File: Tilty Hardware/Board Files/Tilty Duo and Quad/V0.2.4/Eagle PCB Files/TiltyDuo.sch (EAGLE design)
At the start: 45 parts, among them U1 TEENSY_3.0_OUTER-PINS28-DIP_S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, U2 HC-09_BREAKOUT, U3 MPL3115A2LGA8, U4 LM2931, U5 MPU-6050, U6 HMC5883LSMD, U7 SPI_FLASH-X25XXSMD

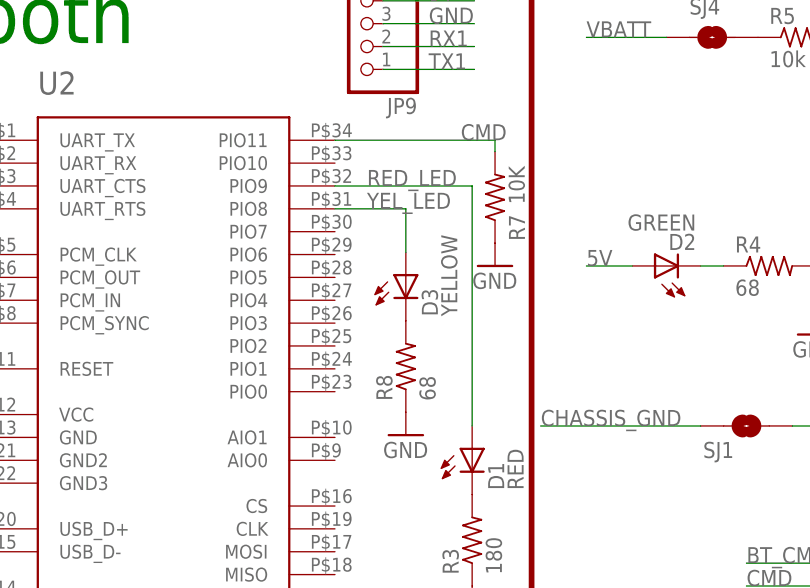
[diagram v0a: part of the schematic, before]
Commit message: Tweaked LED order on Duo/Quad, added lots of memory testing (libraries to come soon)
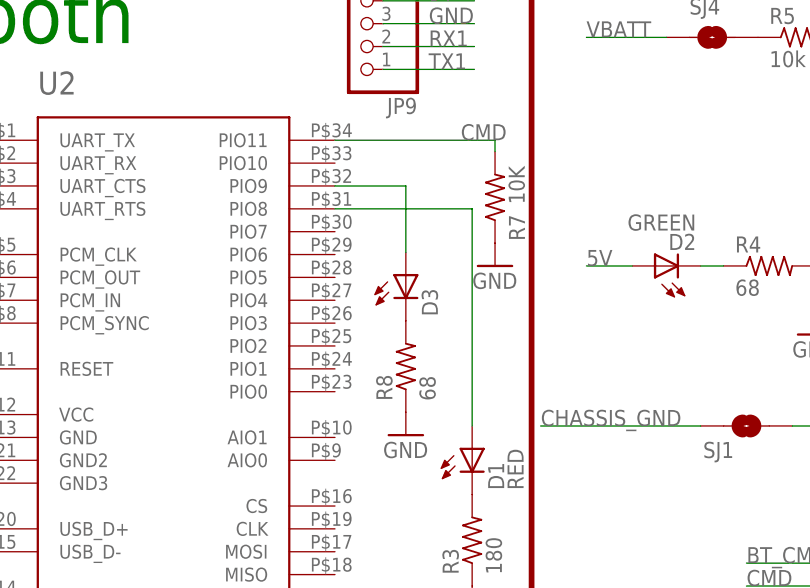
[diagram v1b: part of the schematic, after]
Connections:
- removed net RED_LED: D1.A, U2.PIO9
- new net N$14: D1.A, U2.PIO8
- net YEL_LED: now also U2.PIO9; no longer U2.PIO8
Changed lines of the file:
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@@
 <?xml version="1.0" encoding="utf-8"?>
 <!DOCTYPE eagle SYSTEM "eagle.dtd">
-<eagle version="6.4">
+<eagle version="6.5.0">
 <drawing>
 <settings>
@@
 <instance part="D3" gate="G$1" x="73.914" y="42.164" smashed="yes">
 <attribute name="NAME" x="77.47" y="37.592" size="1.778" layer="95" rot="R90"/>
-<attribute name="VALUE" x="79.629" y="37.592" size="1.778" layer="96" rot="R90"/>
 </instance>
 <instance part="GND7" gate="1" x="73.914" y="24.384"/>
@@
 </segment>
 </net>
-<net name="RED_LED" class="0">
-<segment>
+<net name="YEL_LED" class="0">
+<segment>
+<pinref part="D3" gate="G$1" pin="A"/>
+<wire x1="73.914" y1="52.07" x2="73.914" y2="44.704" width="0.1524" layer="91"/>
 <pinref part="U2" gate="G$1" pin="PIO9"/>
-<wire x1="66.04" y1="52.07" x2="81.28" y2="52.07" width="0.1524" layer="91"/>
-<label x="69.596" y="52.07" size="1.778" layer="95"/>
-<pinref part="D1" gate="G$1" pin="A"/>
-<wire x1="81.28" y1="25.4" x2="81.28" y2="52.07" width="0.1524" layer="91"/>
-</segment>
-</net>
-<net name="YEL_LED" class="0">
-<segment>
-<pinref part="U2" gate="G$1" pin="PIO8"/>
-<wire x1="66.04" y1="49.53" x2="73.914" y2="49.53" width="0.1524" layer="91"/>
-<label x="69.596" y="49.53" size="1.778" layer="95"/>
-<pinref part="D3" gate="G$1" pin="A"/>
-<wire x1="73.914" y1="49.53" x2="73.914" y2="44.704" width="0.1524" layer="91"/>
+<wire x1="73.914" y1="52.07" x2="66.04" y2="52.07" width="0.1524" layer="91"/>
 </segment>
 </net>
@@
 </segment>
 </net>
+<net name="N$14" class="0">
+<segment>
+<pinref part="D1" gate="G$1" pin="A"/>
+<wire x1="81.28" y1="25.4" x2="81.28" y2="49.53" width="0.1524" layer="91"/>
+<pinref part="U2" gate="G$1" pin="PIO8"/>
+<wire x1="81.28" y1="49.53" x2="66.04" y2="49.53" width="0.1524" layer="91"/>
+</segment>
+</net>

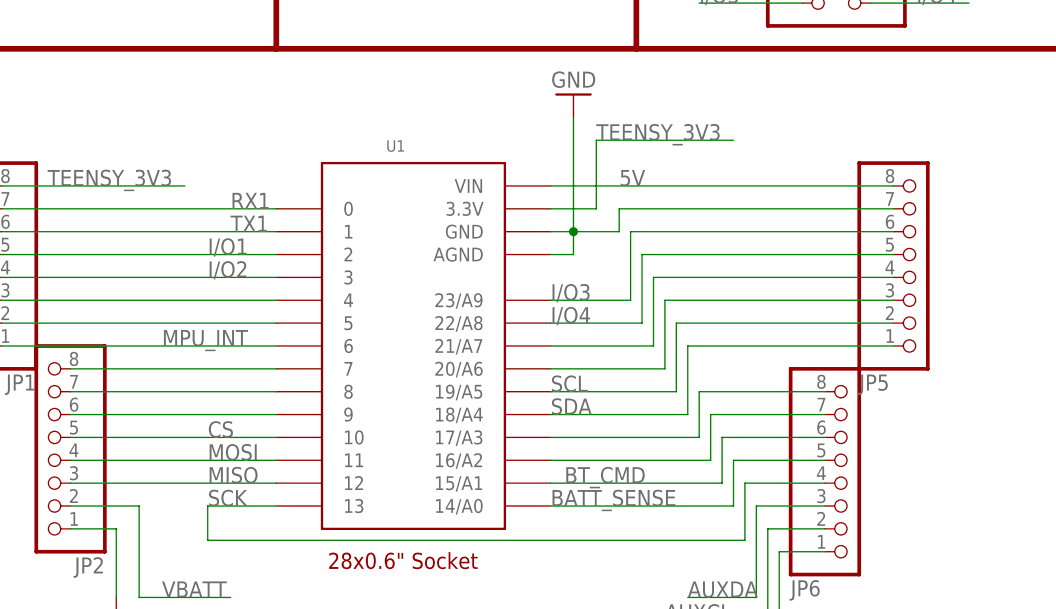
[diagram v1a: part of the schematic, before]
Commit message: Updated Altimeter library to take data pointers as well as return data
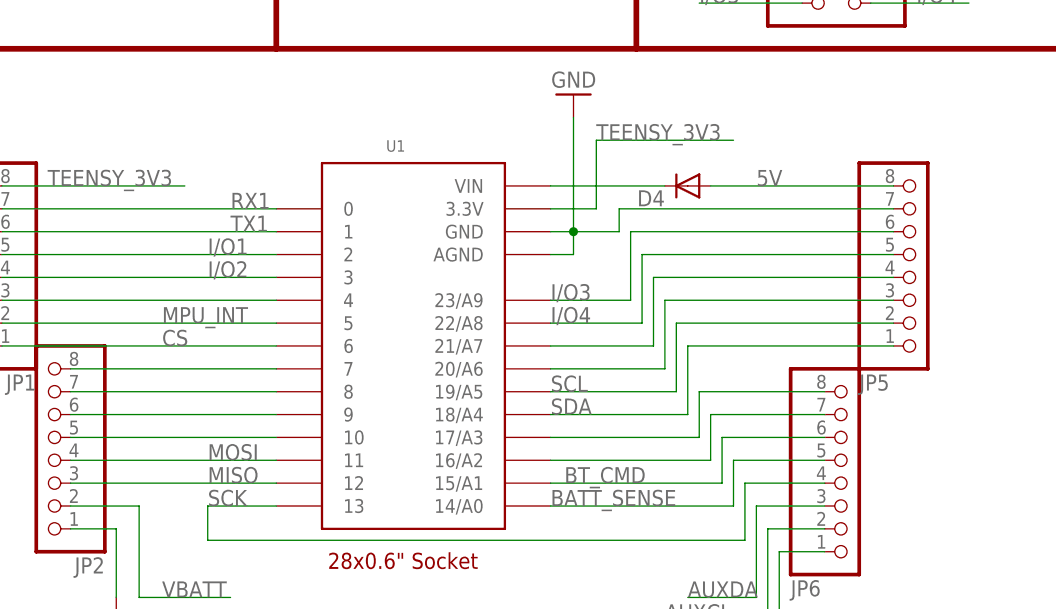
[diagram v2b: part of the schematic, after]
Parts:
- added D4: (no value), SparkFun-DiscreteSemi:DIODESOT23
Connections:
- new net N$15: D4.C, U1.VIN
- net 5V: now also D4.A; no longer U1.VIN
- net CS: now also JP1.1, U1.6; no longer JP2.5, U1.10
- net MPU_INT: now also JP1.2, U1.5; no longer JP1.1, U1.6
- net N$8: now also JP2.5, U1.10; no longer JP1.2, U1.5
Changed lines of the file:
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@@
 <part name="SJ4" library="SparkFun-Passives" deviceset="SOLDERJUMPER" device="TRACE"/>
 <part name="SJ5" library="SparkFun-Passives" deviceset="JUMPER-2" device="SMD-NC"/>
+<part name="D4" library="SparkFun-DiscreteSemi" deviceset="DIODE" device="SOT23"/>
 </parts>
 <sheets>
@@
 </instance>
 <instance part="SJ5" gate="A" x="129.54" y="10.16" rot="R270"/>
+<instance part="D4" gate="G$1" x="218.44" y="60.96" rot="R180"/>
 </instances>
 <busses>
@@
 </segment>
 <segment>
-<pinref part="U1" gate="G$1" pin="6"/>
-<wire x1="172.72" y1="43.18" x2="142.24" y2="43.18" width="0.1524" layer="91"/>
-<pinref part="JP1" gate="A" pin="1"/>
-<label x="160.02" y="43.18" size="1.778" layer="95"/>
+<pinref part="U1" gate="G$1" pin="5"/>
+<wire x1="172.72" y1="45.72" x2="142.24" y2="45.72" width="0.1524" layer="91"/>
+<pinref part="JP1" gate="A" pin="2"/>
+<label x="160.02" y="45.72" size="1.778" layer="95"/>
 </segment>
 </net>
@@
 </segment>
 <segment>
-<pinref part="U1" gate="G$1" pin="VIN"/>
-<pinref part="JP5" gate="A" pin="8"/>
-<wire x1="203.2" y1="60.96" x2="241.3" y2="60.96" width="0.1524" layer="91"/>
-<label x="210.82" y="60.96" size="1.778" layer="95"/>
-</segment>
-<segment>
 <wire x1="99.06" y1="43.18" x2="93.98" y2="43.18" width="0.1524" layer="91"/>
 <label x="93.98" y="43.18" size="1.778" layer="95"/>
@@
 <label x="246.38" y="121.92" size="1.778" layer="95"/>
 </segment>
+<segment>
+<pinref part="D4" gate="G$1" pin="A"/>
+<pinref part="JP5" gate="A" pin="8"/>
+<wire x1="220.98" y1="60.96" x2="241.3" y2="60.96" width="0.1524" layer="91"/>
+<label x="226.06" y="60.96" size="1.778" layer="95"/>
+</segment>
 </net>
 <net name="N$7" class="0">
@@
 <wire x1="172.72" y1="48.26" x2="142.24" y2="48.26" width="0.1524" layer="91"/>
 <pinref part="JP1" gate="A" pin="3"/>
-</segment>
-</net>
-<net name="N$8" class="0">
-<segment>
-<pinref part="U1" gate="G$1" pin="5"/>
-<wire x1="172.72" y1="45.72" x2="142.24" y2="45.72" width="0.1524" layer="91"/>
-<pinref part="JP1" gate="A" pin="2"/>
 </segment>
 </net>
@@
 </segment>
 <segment>
-<pinref part="U1" gate="G$1" pin="10"/>
-<wire x1="149.86" y1="33.02" x2="172.72" y2="33.02" width="0.1524" layer="91"/>
-<pinref part="JP2" gate="A" pin="5"/>
-<label x="165.1" y="33.02" size="1.778" layer="95"/>
+<pinref part="U1" gate="G$1" pin="6"/>
+<wire x1="172.72" y1="43.18" x2="142.24" y2="43.18" width="0.1524" layer="91"/>
+<pinref part="JP1" gate="A" pin="1"/>
+<label x="160.02" y="43.18" size="1.778" layer="95"/>
 </segment>
 </net>
@@
 </segment>
 </net>
+<net name="N$8" class="0">
+<segment>
+<pinref part="JP2" gate="A" pin="5"/>
+<pinref part="U1" gate="G$1" pin="10"/>
+<wire x1="149.86" y1="33.02" x2="172.72" y2="33.02" width="0.1524" layer="91"/>
+</segment>
+</net>
+<net name="N$15" class="0">
+<segment>
+<pinref part="D4" gate="G$1" pin="C"/>
+<pinref part="U1" gate="G$1" pin="VIN"/>
+<wire x1="215.9" y1="60.96" x2="203.2" y2="60.96" width="0.1524" layer="91"/>
+</segment>
+</net>

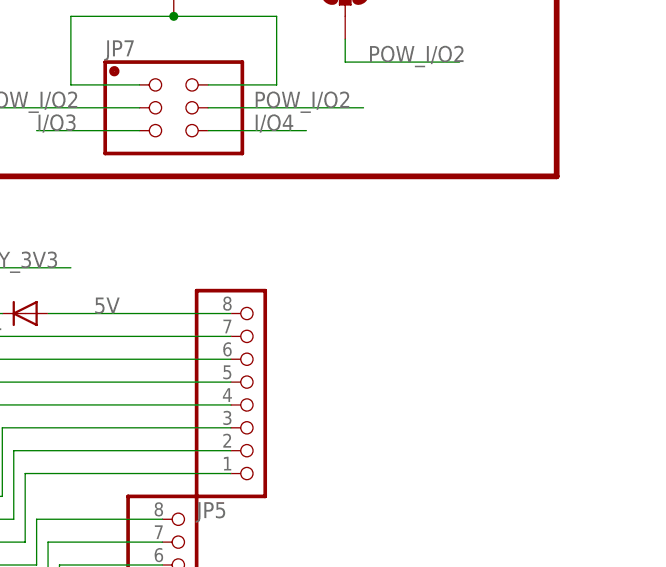
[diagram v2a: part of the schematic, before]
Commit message: Updated Tilty Duo/Quad PCB and TiltyIMU software library
PCB: Added circuit protection
Software: Fixed conflicts with duplicate file names
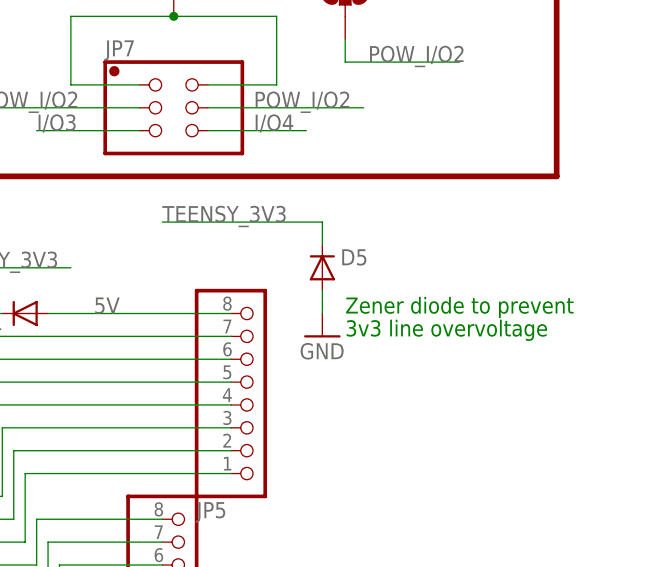
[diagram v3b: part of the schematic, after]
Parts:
- added D5: (no value), SparkFun-DiscreteSemi:DIODESOT23
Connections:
- net GND: now also D5.A
- net TEENSY_3V3: now also D5.C
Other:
- note added: "3v3 line overvoltage"
- note added: "Zener diode to prevent"
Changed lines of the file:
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@@
 <part name="SJ5" library="SparkFun-Passives" deviceset="JUMPER-2" device="SMD-NC"/>
 <part name="D4" library="SparkFun-DiscreteSemi" deviceset="DIODE" device="SOT23"/>
+<part name="D5" library="SparkFun-DiscreteSemi" deviceset="DIODE" device="SOT23">
+<attribute name="PART#" value="BZX84C3V3LT1GOSCT-ND"/>
+</part>
+<part name="GND23" library="supply1" deviceset="GND" device=""/>
 </parts>
 <sheets>
@@
 <wire x1="182.88" y1="193.04" x2="252.222" y2="193.04" width="0.635" layer="94"/>
 <text x="190.5" y="185.42" size="5.08" layer="91" ratio="14">Flash Memory</text>
+<text x="254" y="60.96" size="1.778" layer="91">Zener diode to prevent</text>
+<text x="254" y="58.42" size="1.778" layer="91">3v3 line overvoltage</text>
 </plain>
 <instances>
@@
 <instance part="SJ5" gate="A" x="129.54" y="10.16" rot="R270"/>
 <instance part="D4" gate="G$1" x="218.44" y="60.96" rot="R180"/>
+<instance part="D5" gate="G$1" x="251.46" y="66.04" smashed="yes" rot="R90">
+<attribute name="NAME" x="256.54" y="68.0974" size="1.778" layer="95" rot="R180"/>
+<attribute name="VALUE" x="253.7714" y="68.58" size="1.778" layer="96" rot="R90"/>
+<attribute name="PART#" x="251.46" y="66.04" size="1.778" layer="96" rot="R90" display="off"/>
+</instance>
+<instance part="GND23" gate="1" x="251.46" y="58.42"/>
 </instances>
 <busses>
@@
 <wire x1="190.5" y1="160.02" x2="200.66" y2="160.02" width="0.1524" layer="91"/>
 <junction x="200.66" y="160.02"/>
+</segment>
+<segment>
+<pinref part="D5" gate="G$1" pin="A"/>
+<pinref part="GND23" gate="1" pin="GND"/>
+<wire x1="251.46" y1="60.96" x2="251.46" y2="63.5" width="0.1524" layer="91"/>
 </segment>
 </net>
@@
 <junction x="200.66" y="175.26"/>
 </segment>
-</net>
+<segment>
+<pinref part="D5" gate="G$1" pin="C"/>
+<wire x1="251.46" y1="68.58" x2="251.46" y2="71.12" width="0.1524" layer="91"/>
+<wire x1="251.46" y1="71.12" x2="233.68" y2="71.12" width="0.1524" layer="91"/>
+<label x="233.68" y="71.12" size="1.778" layer="95"/>
+</segment>
+</net>

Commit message: Designed test PCB to surface mount Teensy. Also worked on compass calibration
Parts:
- D4: PART# (none) -> BAT54FSTR-ND
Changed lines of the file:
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@@
 <part name="SJ4" library="SparkFun-Passives" deviceset="SOLDERJUMPER" device="TRACE"/>
 <part name="SJ5" library="SparkFun-Passives" deviceset="JUMPER-2" device="SMD-NC"/>
-<part name="D4" library="SparkFun-DiscreteSemi" deviceset="DIODE" device="SOT23"/>
+<part name="D4" library="SparkFun-DiscreteSemi" deviceset="DIODE" device="SOT23">
+<attribute name="PART#" value="BAT54FSTR-ND"/>
+</part>
 <part name="D5" library="SparkFun-DiscreteSemi" deviceset="DIODE" device="SOT23">
 <attribute name="PART#" value="BZX84C3V3LT1GOSCT-ND"/>
@@
 </instance>
 <instance part="SJ5" gate="A" x="129.54" y="10.16" rot="R270"/>
-<instance part="D4" gate="G$1" x="218.44" y="60.96" rot="R180"/>
+<instance part="D4" gate="G$1" x="218.44" y="60.96" rot="R180">
+<attribute name="PART#" x="218.44" y="60.96" size="1.778" layer="96" rot="R180" display="off"/>
+</instance>
 <instance part="D5" gate="G$1" x="251.46" y="66.04" smashed="yes" rot="R90">
 <attribute name="NAME" x="256.54" y="68.0974" size="1.778" layer="95" rot="R180"/>

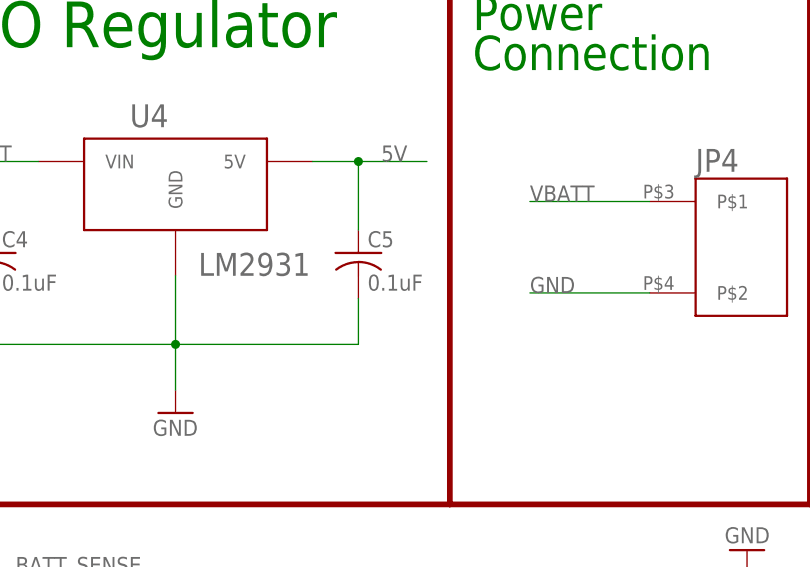
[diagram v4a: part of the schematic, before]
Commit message: Added lots of stuff!
Added a completed Advanced IMU add-on prototype
Added a Spektrum Satellite R/C receiver library
Added Spektrum Satellite R/C receiver testing code
Added a Tilty PCB template
Fixed a bug in the PID library
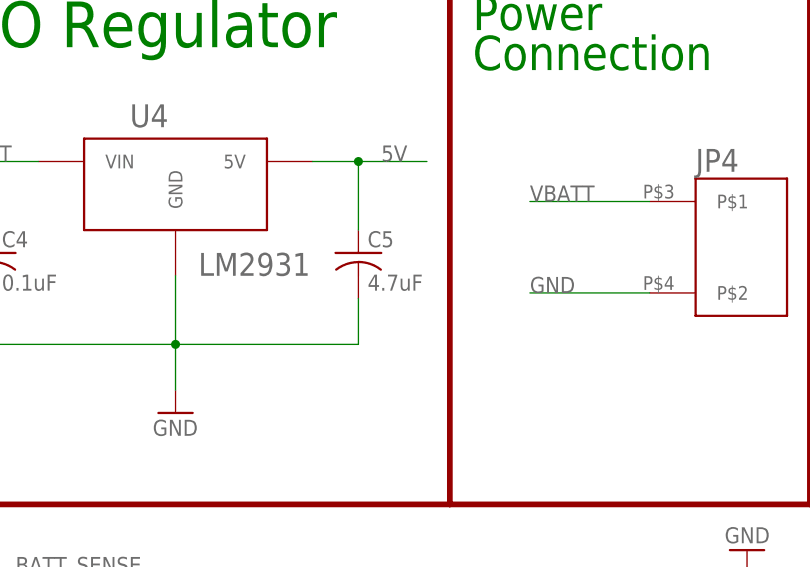
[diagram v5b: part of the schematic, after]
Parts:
- C5: value 0.1uF -> 4.7uF
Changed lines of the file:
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@@
 </part>
 <part name="C4" library="resistor" deviceset="C-US" device="C0603" value="0.1uF"/>
-<part name="C5" library="resistor" deviceset="C-US" device="C0603" value="0.1uF"/>
+<part name="C5" library="resistor" deviceset="C-US" device="C0603" value="4.7uF"/>
 <part name="U1" library="My Parts" deviceset="TEENSY_3.0_OUTER-PINS" device="28-DIP_SOCKET">
 <attribute name="COST" value="0.28"/>
@@
 </part>
 <part name="GND23" library="supply1" deviceset="GND" device=""/>
+<part name="U$1" library="My Parts" deviceset="JST_ZH_PTH_CONNECTOR" device=""/>
+<part name="U$2" library="My Parts" deviceset="JST_ZH_PTH_CONNECTOR" device=""/>
+<part name="U$3" library="My Parts" deviceset="JST_ZH_PTH_CONNECTOR" device=""/>
+<part name="U$4" library="My Parts" deviceset="JST_ZH_PTH_CONNECTOR" device=""/>
+<part name="U$5" library="My Parts" deviceset="JST_ZH_PTH_CONNECTOR" device=""/>
 </parts>
 <sheets>

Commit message: Tilty PCB work
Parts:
- added D6: (no value), diode:DIODE-DO214AA
- added SJ6: SOLDERJUMPERTRACE, SparkFun-Passives:SOLDERJUMPERTRACE
- JP1, JP2: value (none) -> 8-PIN_HEADER; device pinhead:PINHD-1X81X08_NO_SILK_LOCK -> My Parts:8-PIN_HEADER
- JP3: value (none) -> 8-PIN_HEADER; device pinhead:PINHD-2X32X03_NO_SS_LOCK -> My Parts:8-PIN_HEADER
- JP4: value 2-POS_SMD_TERM_BLOCK -> 8-PIN_HEADER; device My Parts:2-POS_SMD_TERM_BLOCK -> My Parts:8-PIN_HEADER; PART# 277-2337-1-ND -> (none); POSSIBLE_ALT 009276002021106 -> (none)
- JP5: value (none) -> 2-POS_SMD_TERM_BLOCK; device pinhead:PINHD-1X81X08_NO_SILK_LOCK -> My Parts:2-POS_SMD_TERM_BLOCK; PART# (none) -> 277-2337-1-ND; POSSIBLE_ALT (none) -> 009276002021106
- JP6: device pinhead:PINHD-1X81X08_NO_SILK_LOCK -> pinhead:PINHD-2X32X03_NO_SS_LOCK
- SJ2: device SparkFun-Passives:SOLDERJUMPER_2WAYS -> SparkFun-Passives:SOLDERJUMPER_2WAYPASTE1&2
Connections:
- net 5V: now also JP4.1; no longer JP5.8
- net AUXCL: now also JP3.7; no longer JP6.2
- net AUXDA: now also JP3.6; no longer JP6.3
- net BATT_SENSE: now also JP3.4; no longer JP6.5
- net BT_CMD: now also JP3.3; no longer JP6.6
- net GND: now also JP3.8, JP4.2, JP5.P$2, JP6.2; no longer JP3.1, JP3.2, JP4.P$2, JP5.7
- net I/O1: now also JP6.6; no longer JP3.6
- net I/O2: now also JP6.5; no longer JP3.5
- net I/O3: now also JP4.3; no longer JP5.6
- net I/O4: now also JP4.4; no longer JP5.5
- net N$10: now also JP3.1; no longer JP6.8
- net N$18: now also JP4.5; no longer JP5.4
- net N$19: now also JP4.6; no longer JP5.3
- net N$23: now also JP3.2; no longer JP6.7
- net POW_I/O1: now also JP6.3, JP6.4; no longer JP3.3, JP3.4
- net SCK: now also JP3.5; no longer JP6.4
- net SCL: now also JP4.7; no longer JP5.2
- net SDA: now also JP4.8; no longer JP5.1
- net VBATT: now also D6.A, D6.C, JP5.P$1, SJ6.1, SJ6.2; no longer JP4.P$1
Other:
- note added: "Zener diode to ease voltage"
- note added: "regulation at high inputs"

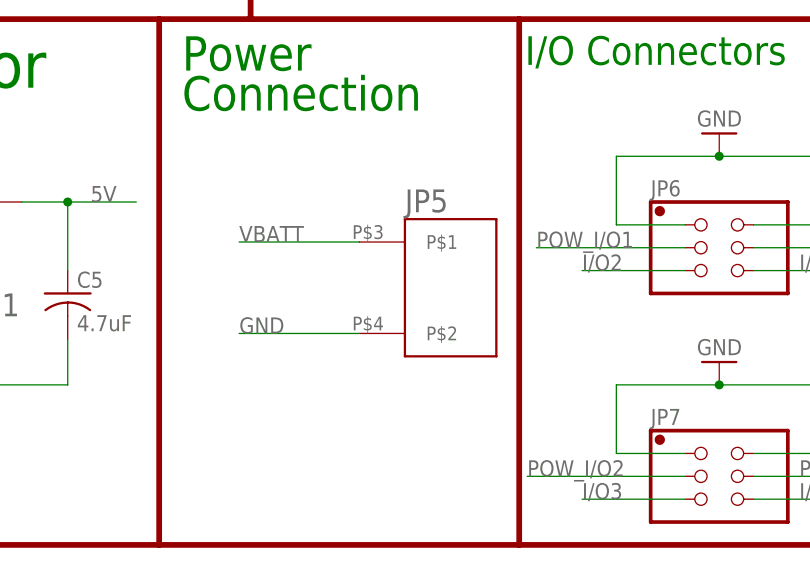
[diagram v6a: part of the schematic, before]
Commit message: Finished Tilty Duo/Quad 0.2.4, work on motor driver
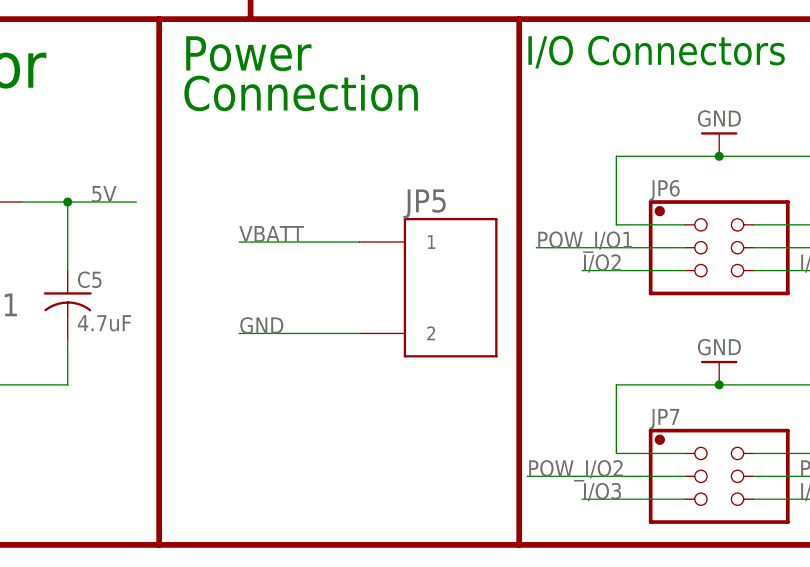
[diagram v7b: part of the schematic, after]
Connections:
- net GND: now also JP5.2; no longer JP5.P$2
- net VBATT: now also JP5.1; no longer JP5.P$1
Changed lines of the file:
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@@
 </segment>
 <segment>
-<pinref part="JP5" gate="G$1" pin="P$2"/>
+<pinref part="JP5" gate="G$1" pin="2"/>
 <wire x1="194.945" y1="99.695" x2="181.61" y2="99.695" width="0.1524" layer="91"/>
 <label x="181.61" y="99.695" size="1.778" layer="95"/>
@@
 <net name="VBATT" class="0">
 <segment>
-<pinref part="JP5" gate="G$1" pin="P$1"/>
+<pinref part="JP5" gate="G$1" pin="1"/>
 <wire x1="194.945" y1="109.855" x2="181.61" y2="109.855" width="0.1524" layer="91"/>
 <label x="181.61" y="109.855" size="1.778" layer="95"/>
